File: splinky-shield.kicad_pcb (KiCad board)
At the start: 2 copper layers, 73.5 x 50.8 mm, 61 parts, among them J1 USB_C_Receptacle_USB2.0, J10 Ribbon, J11 Serial, J12 Conn_01x04_Female, J13 Conn_01x02_Female, J2 Conn_01x04_Female, J3 Conn_01x04_Female, J4 Conn_01x04_Female, J5 Conn_01x02, J6 Serial, J7 trackball, J8 Ribbon, J9 RGB, U1 RP2040, U2 GD25Q80CEIGR, U3 XC6210B332MR-G, U4 USBLC6-2P6, Y1 Crystal_GND24

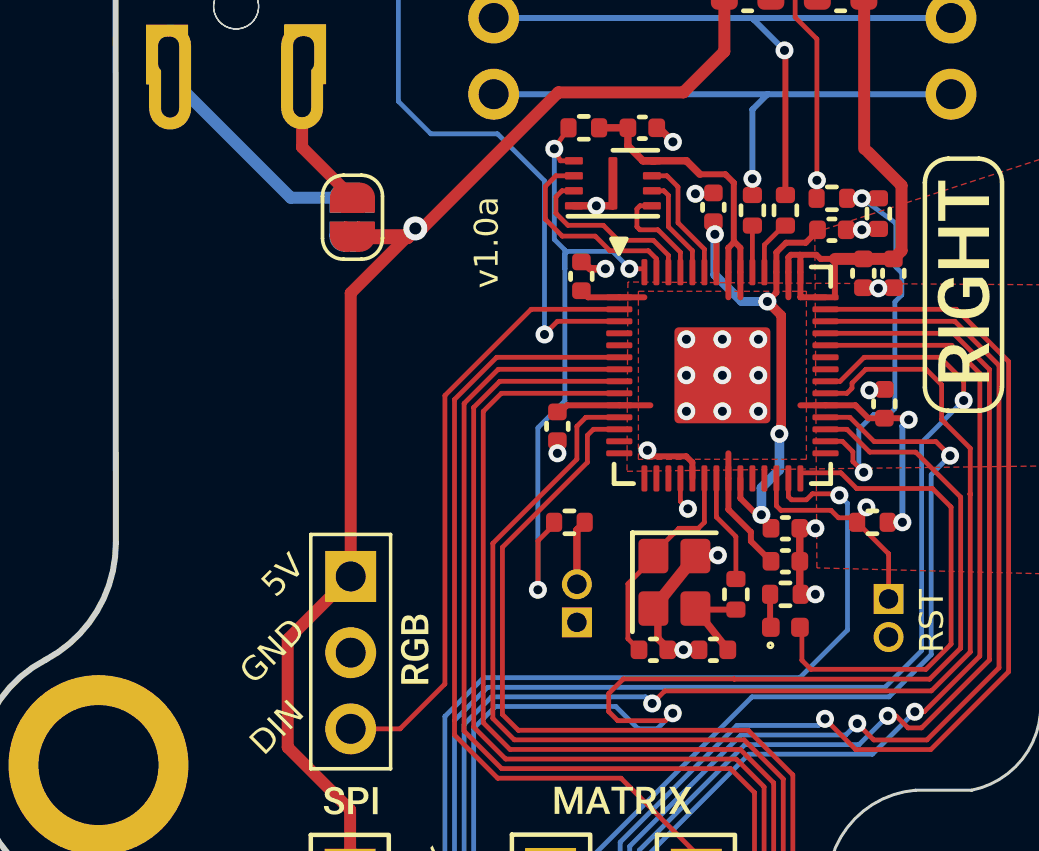
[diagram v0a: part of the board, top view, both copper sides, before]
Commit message: add back rst button
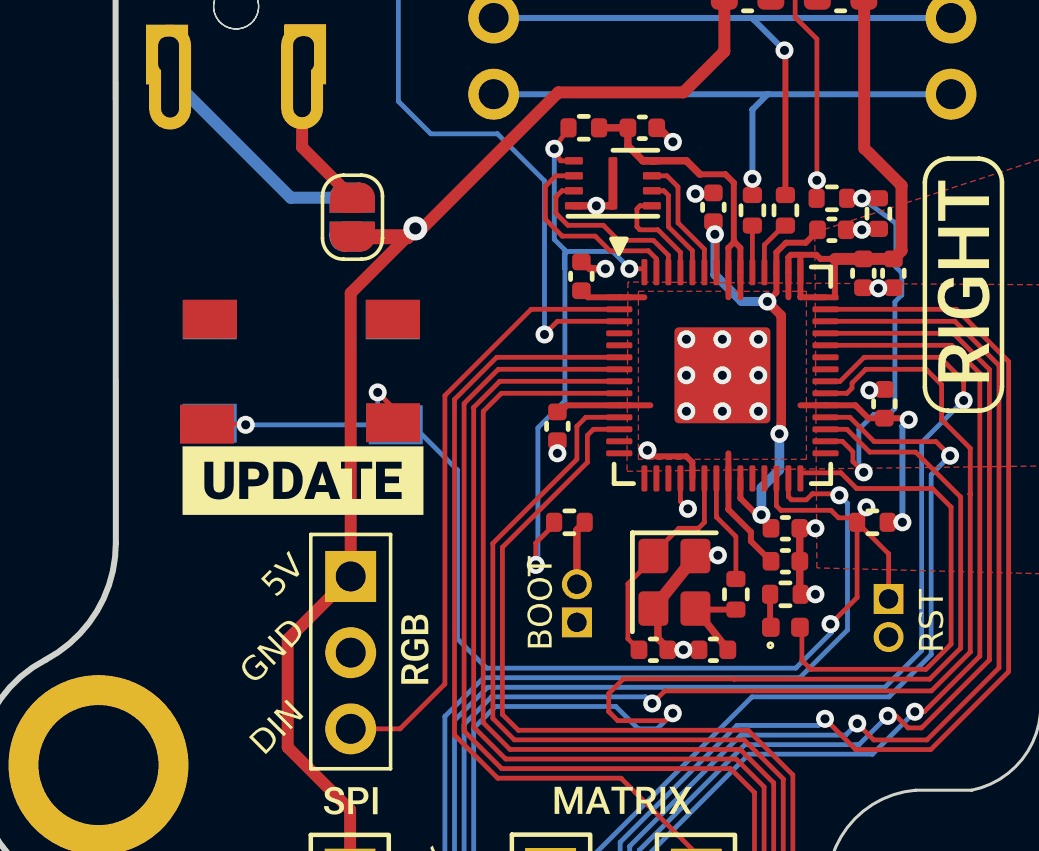
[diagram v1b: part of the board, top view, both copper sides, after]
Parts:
- added SW1: SW_SPST, Library:PushSwitch, F.Cu at (138.3, 96.8)
- added SW2: SW_SPST, Library:PushSwitch, B.Cu at (138.4, 96.8)
- added kibuzzard-61F01C84: G***, kibuzzard-61F01C84, F.Cu at (138.4, 100.5)
- added kibuzzard-61F01C84: G***, kibuzzard-61F01C84, B.Cu at (138.4, 100.5)
- moved G*** 45.0 mm to (188.0, 122.9)
- moved REF** 6.96 mm to (151.3, 94.1)
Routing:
- net /~{RESET}: track 8.01 -> 43.8 mm, vias 1 -> 4
- net /QSPI_~{CS}: track 23.0 -> 21.4 mm
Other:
- board text added: "BOOT"

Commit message: DRC
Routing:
- net ss_l: track 31.9 -> 36.3 mm
- net /~{RESET}: track 43.8 -> 44.7 mm
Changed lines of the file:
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@@
   (segment (start 156.325 97.2) (end 155.8375 97.2) (width 0.16) (layer "F.Cu") (net 22))
   (via (at 160.44194 97.84) (size 0.6) (drill 0.3) (layers "F.Cu" "B.Cu") (net 22))
+  (segment (start 143.47 117.58) (end 143.47 108.50187) (width 0.16) (layer "B.Cu") (net 22))
+  (segment (start 159.28048 99.00146) (end 160.44194 97.84) (width 0.16) (layer "B.Cu") (net 22))
+  (segment (start 143.47 108.50187) (end 144.57235 107.39952) (width 0.16) (layer "B.Cu") (net 22))
+  (segment (start 158.22861 107.39952) (end 159.28048 106.34765) (width 0.16) (layer "B.Cu") (net 22))
   (segment (start 139.99 118.709999) (end 142.340001 118.709999) (width 0.16) (layer "B.Cu") (net 22))
-  (segment (start 157.81861 107.39952) (end 159.04048 106.17765) (width 0.16) (layer "B.Cu") (net 22))
-  (segment (start 143.47 108.50187) (end 144.57235 107.39952) (width 0.16) (layer "B.Cu") (net 22))
-  (segment (start 159.04048 106.17765) (end 159.04048 99.24146) (width 0.16) (layer "B.Cu") (net 22))
-  (segment (start 143.47 117.58) (end 143.47 108.50187) (width 0.16) (layer "B.Cu") (net 22))
-  (segment (start 159.04048 99.24146) (end 160.44194 97.84) (width 0.16) (layer "B.Cu") (net 22))
   (segment (start 142.340001 118.709999) (end 143.47 117.58) (width 0.16) (layer "B.Cu") (net 22))
-  (segment (start 144.57235 107.39952) (end 157.81861 107.39952) (width 0.16) (layer "B.Cu") (net 22))
+  (segment (start 159.28048 106.34765) (end 159.28048 99.00146) (width 0.16) (layer "B.Cu") (net 22))
+  (segment (start 144.57235 107.39952) (end 158.22861 107.39952) (width 0.16) (layer "B.Cu") (net 22))
   (segment (start 156.3 101) (end 156.25 100.95) (width 0.16) (layer "F.Cu") (net 23))
   (segment (start 154.7 101.15) (end 154.6 101.05) (width 0.16) (layer "F.Cu") (net 23))
@@
   (segment (start 156.25 100.95) (end 155.4 100.95) (width 0.16) (layer "F.Cu") (net 23))
   (via (at 156.3 101) (size 0.6) (drill 0.3) (layers "F.Cu" "B.Cu") (net 23))
-  (segment (start 156.57 105.49) (end 154.98 107.08) (width 0.16) (layer "B.Cu") (net 23))
-  (segment (start 141.900001 116.169999) (end 139.99 116.169999) (width 0.16) (layer "B.Cu") (net 23))
-  (segment (start 156.57 101.27) (end 156.57 105.49) (width 0.16) (layer "B.Cu") (net 23))
-  (segment (start 156.3 101) (end 156.57 101.27) (width 0.16) (layer "B.Cu") (net 23))
-  (segment (start 143.15048 114.91952) (end 141.900001 116.169999) (width 0.16) (layer "B.Cu") (net 23))
-  (segment (start 143.15048 108.369521) (end 143.15048 114.91952) (width 0.16) (layer "B.Cu") (net 23))
-  (segment (start 144.44 107.08) (end 143.15048 108.369521) (width 0.16) (layer "B.Cu") (net 23))
-  (segment (start 154.98 107.08) (end 144.44 107.08) (width 0.16) (layer "B.Cu") (net 23))
+  (segment (start 141.900001 116.169999) (end 143.15048 114.91952) (width 0.16) (layer "B.Cu") (net 23))
+  (segment (start 156.57 102.34) (end 156.57 101.27) (width 0.16) (layer "B.Cu") (net 23))
+  (segment (start 158.96096 106.2153) (end 158.96096 103.74096) (width 0.16) (layer "B.Cu") (net 23))
+  (segment (start 158.96096 103.74096) (end 157.96 102.74) (width 0.16) (layer "B.Cu") (net 23))
+  (segment (start 143.15048 108.369521) (end 144.44 107.08) (width 0.16) (layer "B.Cu") (net 23))
+  (segment (start 157.96 102.74) (end 156.97 102.74) (width 0.16) (layer "B.Cu") (net 23))
+  (segment (start 139.99 116.169999) (end 141.900001 116.169999) (width 0.16) (layer "B.Cu") (net 23))
+  (segment (start 156.57 101.27) (end 156.3 101) (width 0.16) (layer "B.Cu") (net 23))
+  (segment (start 143.15048 114.91952) (end 143.15048 108.369521) (width 0.16) (layer "B.Cu") (net 23))
+  (segment (start 156.97 102.74) (end 156.57 102.34) (width 0.16) (layer "B.Cu") (net 23))
+  (segment (start 158.09626 107.08) (end 158.96096 106.2153) (width 0.16) (layer "B.Cu") (net 23))
+  (segment (start 144.44 107.08) (end 158.09626 107.08) (width 0.16) (layer "B.Cu") (net 23))
   (segment (start 145.59614 108.8324) (end 145.0676 108.30386) (width 0.16) (layer "F.Cu") (net 24))
   (segment (start 147.9 99.9) (end 147.9 99) (width 0.16) (layer "F.Cu") (net 24))
@@
   (segment (start 159.52 99.21) (end 157.459139 99.21) (width 0.16) (layer "F.Cu") (net 35))
   (via (at 159.99 99.68) (size 0.6) (drill 0.3) (layers "F.Cu" "B.Cu") (free) (net 35))
-  (segment (start 153.385352 107.71904) (end 157.95096 107.71904) (width 0.16) (layer "B.Cu") (net 35))
+  (segment (start 147.494392 113.61) (end 153.385352 107.71904) (width 0.16) (layer "B.Cu") (net 35))
+  (segment (start 159.6 106.48) (end 159.6 100.07) (width 0.16) (layer "B.Cu") (net 35))
+  (segment (start 153.385352 107.71904) (end 158.36096 107.71904) (width 0.16) (layer "B.Cu") (net 35))
+  (segment (start 159.6 100.07) (end 159.99 99.68) (width 0.16) (layer "B.Cu") (net 35))
+  (segment (start 158.36096 107.71904) (end 159.6 106.48) (width 0.16) (layer "B.Cu") (net 35))
   (segment (start 146.672542 113.61) (end 147.494392 113.61) (width 0.16) (layer "B.Cu") (net 35))
-  (segment (start 159.36 100.31) (end 159.99 99.68) (width 0.16) (layer "B.Cu") (net 35))
-  (segment (start 159.36 106.31) (end 159.36 100.31) (width 0.16) (layer "B.Cu") (net 35))
-  (segment (start 157.95096 107.71904) (end 159.36 106.31) (width 0.16) (layer "B.Cu") (net 35))
-  (segment (start 147.494392 113.61) (end 153.385352 107.71904) (width 0.16) (layer "B.Cu") (net 35))
   (segment (start 140.05 91.08) (end 138.01 91.08) (width 0.4) (layer "B.Cu") (net 36))
   (segment (start 138.01 91.08) (end 133.99 87.06) (width 0.4) (layer "B.Cu") (net 36))
   (segment (start 156.9 101.91) (end 156.74 101.75) (width 0.16) (layer "F.Cu") (net 37))
+  (segment (start 156.258515 102.531485) (end 156.89 101.9) (width 0.16) (layer "F.Cu") (net 37))
   (segment (start 156.89 101.9) (end 157.94 102.95) (width 0.16) (layer "F.Cu") (net 37))
+  (segment (start 156.4305 105.91) (end 156.258515 105.738015) (width 0.16) (layer "F.Cu") (net 37))
   (segment (start 154.35 101.5) (end 154.2 101.35) (width 0.16) (layer "F.Cu") (net 37))
-  (segment (start 156.89 101.9) (end 156.89 104.40703) (width 0.16) (layer "F.Cu") (net 37))
   (segment (start 157.2 101.4) (end 156.89 101.9) (width 0.25) (layer "F.Cu") (net 37))
   (segment (start 156.269553 101.75) (end 156.019553 101.5) (width 0.16) (layer "F.Cu") (net 37))
   (segment (start 136.49 98.63) (end 136.51 98.65) (width 0.16) (layer "F.Cu") (net 37))
   (segment (start 154.2 101.35) (end 154.2 100.4375) (width 0.16) (layer "F.Cu") (net 37))
-  (segment (start 156.89 104.40703) (end 156.003765 105.293265) (width 0.16) (layer "F.Cu") (net 37))
   (segment (start 157.2 101.4) (end 156.9 101.91) (width 0.16) (layer "F.Cu") (net 37))
   (segment (start 157.94 102.95) (end 157.94 104.455) (width 0.16) (layer "F.Cu") (net 37))
   (segment (start 141.42 98.08) (end 140.91 97.57) (width 0.16) (layer "F.Cu") (net 37))
+  (segment (start 156.258515 105.738015) (end 156.258515 102.531485) (width 0.16) (layer "F.Cu") (net 37))
   (segment (start 141.42 98.58) (end 141.42 98.08) (width 0.16) (layer "F.Cu") (net 37))
   (segment (start 156.74 101.75) (end 156.269553 101.75) (width 0.16) (layer "F.Cu") (net 37))
   (segment (start 156.019553 101.5) (end 154.35 101.5) (width 0.16) (layer "F.Cu") (net 37))
   (segment (start 135.22 98.63) (end 136.49 98.63) (width 0.16) (layer "F.Cu") (net 37))
-  (via (at 156.003765 105.293265) (size 0.6) (drill 0.3) (layers "F.Cu" "B.Cu") (net 37))
+  (via (at 156.4305 105.91) (size 0.6) (drill 0.3) (layers "F.Cu" "B.Cu") (net 37))
   (via (at 136.51 98.65) (size 0.6) (drill 0.3) (layers "F.Cu" "B.Cu") (net 37))
   (via (at 140.91 97.57) (size 0.6) (drill 0.3) (layers "F.Cu" "B.Cu") (net 37))
   (via (at 157.2 101.4) (size 0.6) (drill 0.3) (layers "F.Cu" "B.Cu") (net 37))
-  (segment (start 156.04 105.56813) (end 154.84765 106.76048) (width 0.16) (layer "B.Cu") (net 37))
+  (segment (start 156.04765 106.76048) (end 156.474065 106.334065) (width 0.16) (layer "B.Cu") (net 37))
+  (segment (start 156.474065 106.334065) (end 156.474065 105.953565) (width 0.16) (layer "B.Cu") (net 37))
   (segment (start 135.36 98.65) (end 135.31 98.6) (width 0.16) (layer "B.Cu") (net 37))
-  (segment (start 156.003765 105.293265) (end 156.04 105.3295) (width 0.16) (layer "B.Cu") (net 37))
-  (segment (start 143.57 105.79) (end 143.57 100.16) (width 0.16) (layer "B.Cu") (net 37))
+  (segment (start 144.54048 106.76048) (end 156.04765 106.76048) (width 0.16) (layer "B.Cu") (net 37))
   (segment (start 140.91 98.05) (end 141.51 98.65) (width 0.16) (layer "B.Cu") (net 37))
+  (segment (start 143.57 100.16) (end 143.57 105.79) (width 0.16) (layer "B.Cu") (net 37))
+  (segment (start 156.474065 105.953565) (end 156.4305 105.91) (width 0.16) (layer "B.Cu") (net 37))
+  (segment (start 143.57 105.79) (end 144.54048 106.76048) (width 0.16) (layer "B.Cu") (net 37))
   (segment (start 141.51 98.65) (end 136.51 98.65) (width 0.16) (layer "B.Cu") (net 37))
-  (segment (start 142.06 98.65) (end 141.51 98.65) (width 0.16) (layer "B.Cu") (net 37))
+  (segment (start 141.51 98.65) (end 142.06 98.65) (width 0.16) (layer "B.Cu") (net 37))
   (segment (start 140.91 97.57) (end 140.91 98.05) (width 0.16) (layer "B.Cu") (net 37))
-  (segment (start 144.54048 106.76048) (end 143.57 105.79) (width 0.16) (layer "B.Cu") (net 37))
   (segment (start 136.51 98.65) (end 135.36 98.65) (width 0.16) (layer "B.Cu") (net 37))
-  (segment (start 154.84765 106.76048) (end 144.54048 106.76048) (width 0.16) (layer "B.Cu") (net 37))
-  (segment (start 143.57 100.16) (end 142.06 98.65) (width 0.16) (layer "B.Cu") (net 37))
-  (segment (start 156.04 105.3295) (end 156.04 105.56813) (width 0.16) (layer "B.Cu") (net 37))
+  (segment (start 142.06 98.65) (end 143.57 100.16) (width 0.16) (layer "B.Cu") (net 37))
   (segment (start 151 101.2) (end 151.25 101.45) (width 0.16) (layer "F.Cu") (net 38))
   (segment (start 151 100.4375) (end 151 101.2) (width 0.16) (layer "F.Cu") (net 38))
